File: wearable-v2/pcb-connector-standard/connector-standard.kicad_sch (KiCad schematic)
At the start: 35 parts, among them J1 HERALD_V2_CONN_RECEPTACLE, J11 PNL_1, J12 PNL_2, J13 PNL_3, J14 PNL_4, J2 HERALD_V2_CONN_RECEPTACLE, J3 HERALD_V2_CONN_RECEPTACLE, J4 HERALD_V2_CONN_RECEPTACLE, J7 USB_C_Receptacle_USB2.0, U1 DT1446-04V, U15 TLV751, U2 MCP73831/2-2MC, U3 TCA6408A, U4 FT201XQ

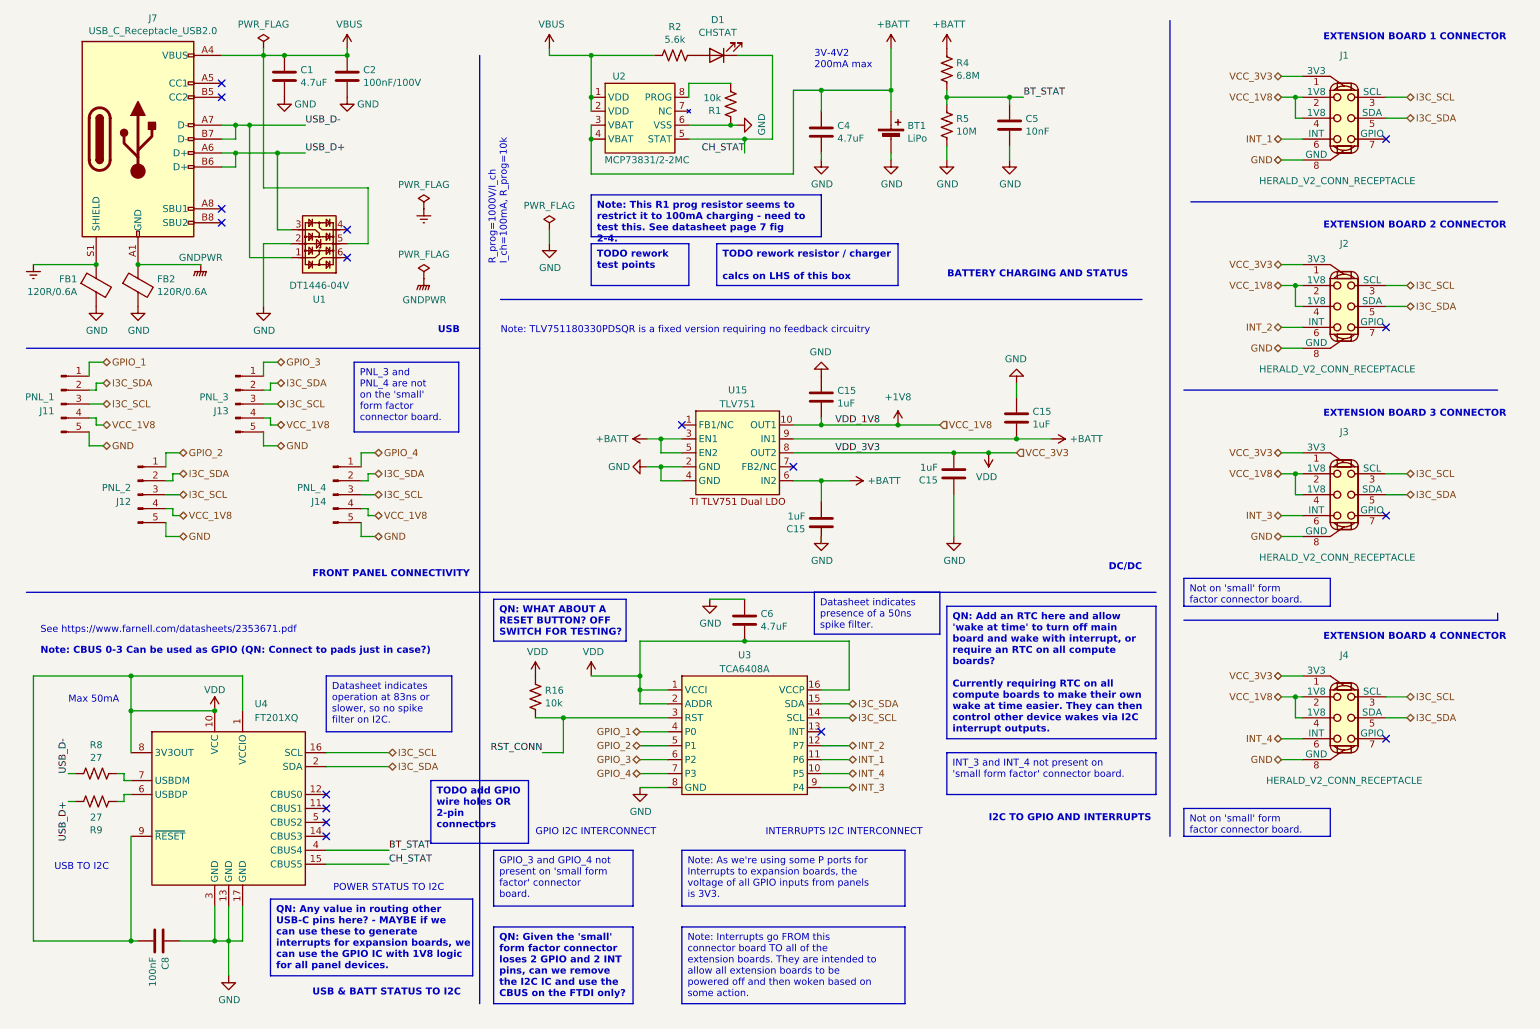
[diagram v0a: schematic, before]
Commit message: Refactoring PCB files
Moved major boards into their own files.
Corrected design elements for PCBWay manufacture.
Signed-off-by: Adam Fowler <adam@adamfowler.org>
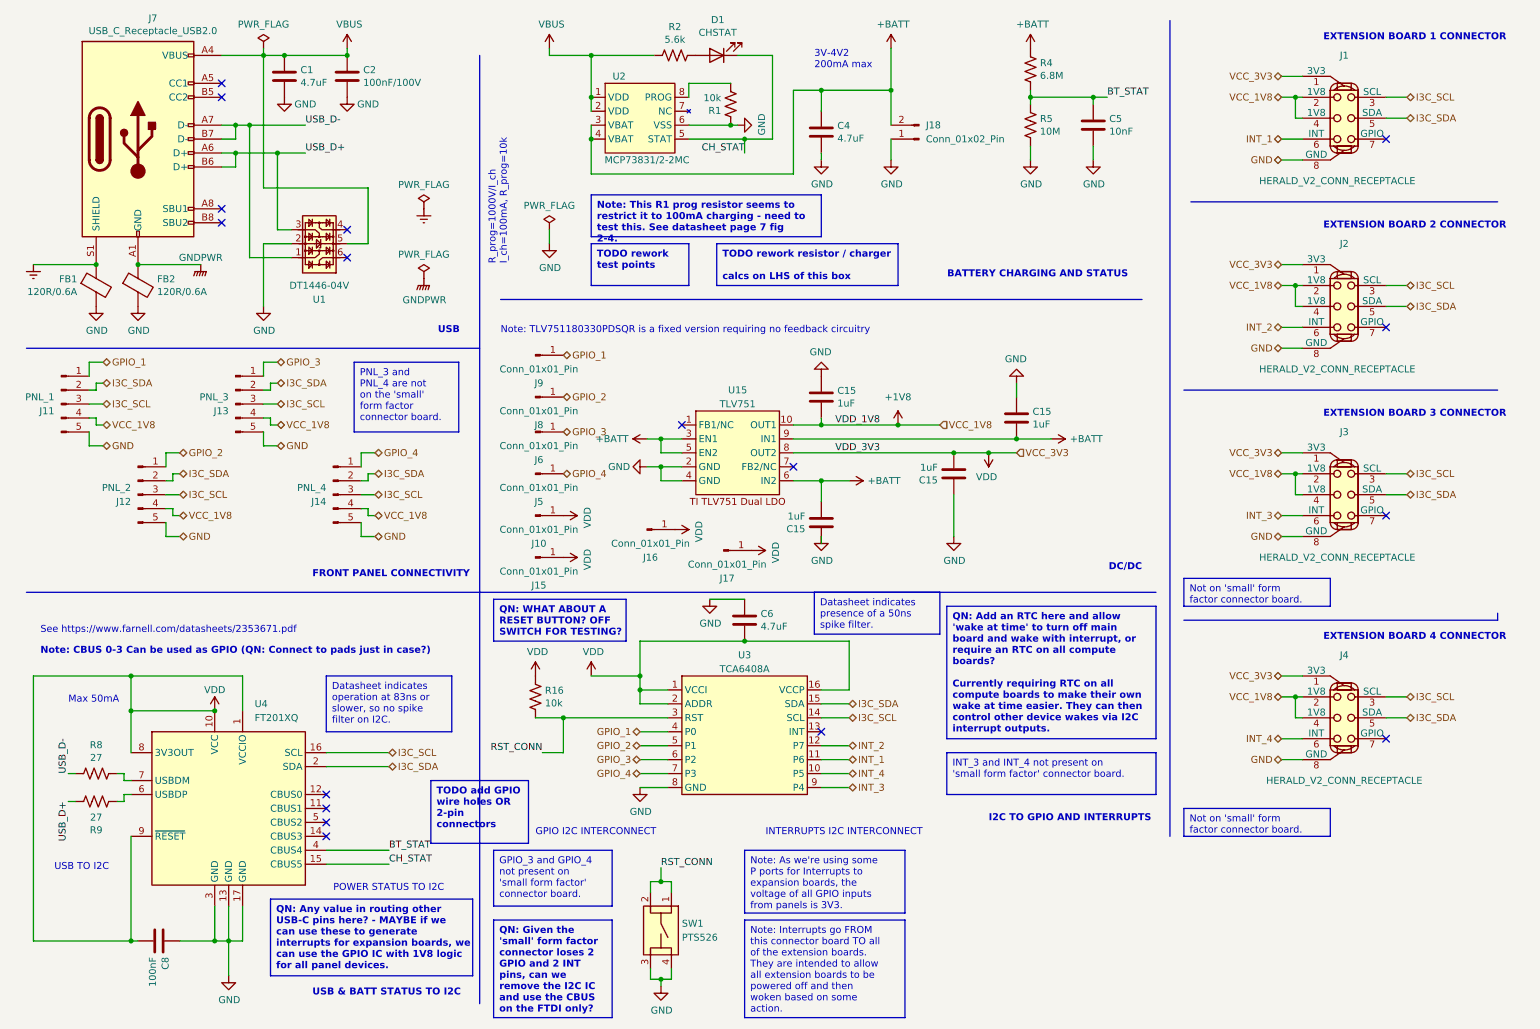
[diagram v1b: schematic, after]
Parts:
- removed BT1: LiPo, Herald:Herald_Battery_Solder_Pads, symbol Device:Battery_Cell
- added J10, J15, J16, J17, J5, J6, J8, J9: Conn_01x01_Pin, Connector_PinHeader_1.00mm:PinHeader_1x01_P1.00mm_Vertical, symbol Connector:Conn_01x01_Pin
- added J18: Conn_01x02_Pin, Connector_PinHeader_1.00mm:PinHeader_1x02_P1.00mm_Vertical, symbol Connector:Conn_01x02_Pin
- added SW1: PTS526, Herald:PTS526, symbol Herald_Extras:SPST_NO_RESET
- J1, J2, J3, J4: MPN (none) -> 245861006004829+
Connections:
- net +BATT: now also J18.2 (Pin_2)
- net GND: now also J18.1 (Pin_1), SW1.3, SW1.4
- net GPIO_1: now also J9.1 (Pin_1)
- net GPIO_2: now also J8.1 (Pin_1)
- net GPIO_3: now also J6.1 (Pin_1)
- net GPIO_4: now also J5.1 (Pin_1)
- net RST_CONN: now also SW1.1, SW1.2
- net VDD: now also J10.1 (Pin_1), J15.1 (Pin_1), J16.1 (Pin_1), J17.1 (Pin_1)
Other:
- moved on the sheet: C5, R4, R5

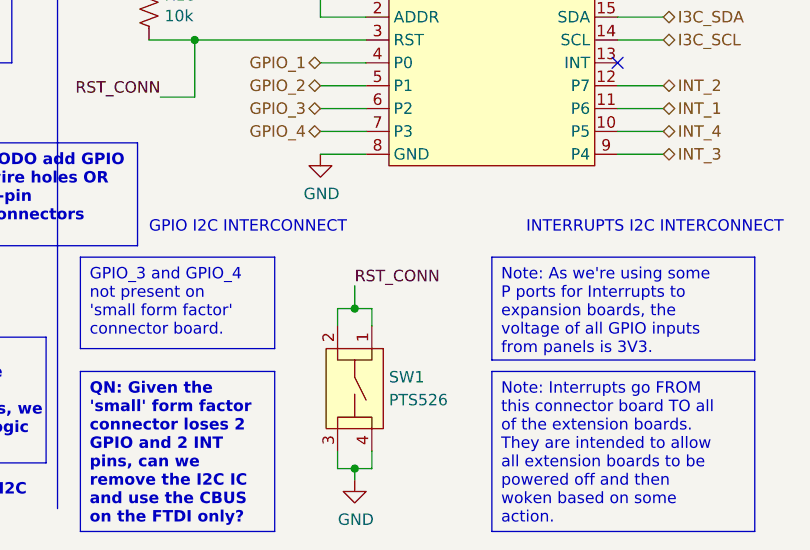
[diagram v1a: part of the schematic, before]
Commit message: Reworked boards for JLCPCB manufacture
Slightly larger Vias.
Added debug pin holes for Beta testing.
Signed-off-by: Adam Fowler <adam@adamfowler.org>
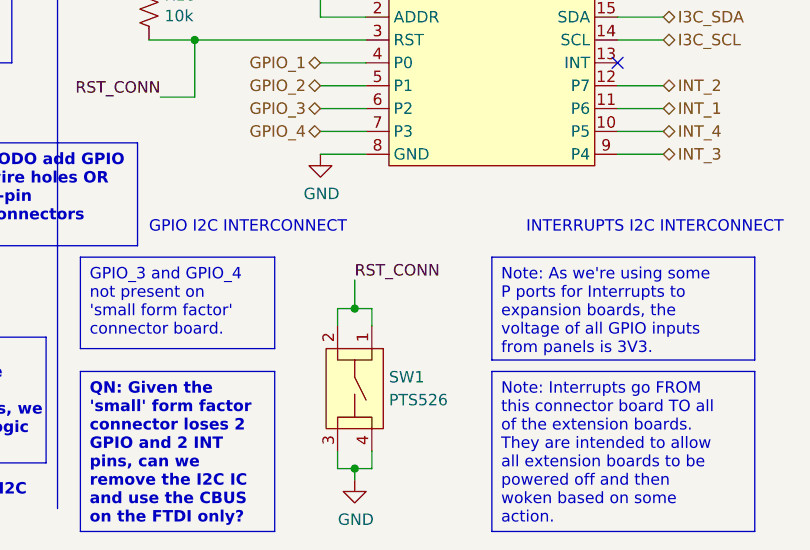
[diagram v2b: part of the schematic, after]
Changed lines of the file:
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@@
     (stroke (width 0) (type default))
   )
-  (wire (pts (xy 129.54 169.545) (xy 129.54 172.085))
+  (wire (pts (xy 129.54 168.91) (xy 129.54 172.085))
     (stroke (width 0) (type default))
   )
@@
     (effects (font (size 1.27 1.27)) (justify right bottom))
   )
-  (label "RST_CONN" (at 129.54 169.545 0) (fields_autoplaced)
-    (effects (font (size 1.27 1.27)) (justify left bottom))
-  )
+  (label "RST_CONN" (at 129.54 168.91 0) (fields_autoplaced)
+    (effects (font (size 1.27 1.27)) (justify left bottom))
+  )
